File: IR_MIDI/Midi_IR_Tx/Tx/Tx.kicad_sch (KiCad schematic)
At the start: 16 parts, among them J1 MIDI in, J2 MIDI Thr, Q1 2N3904, Q2 2N3904, Q3 2N3904, Q4 2N3904, Y1 1MHz

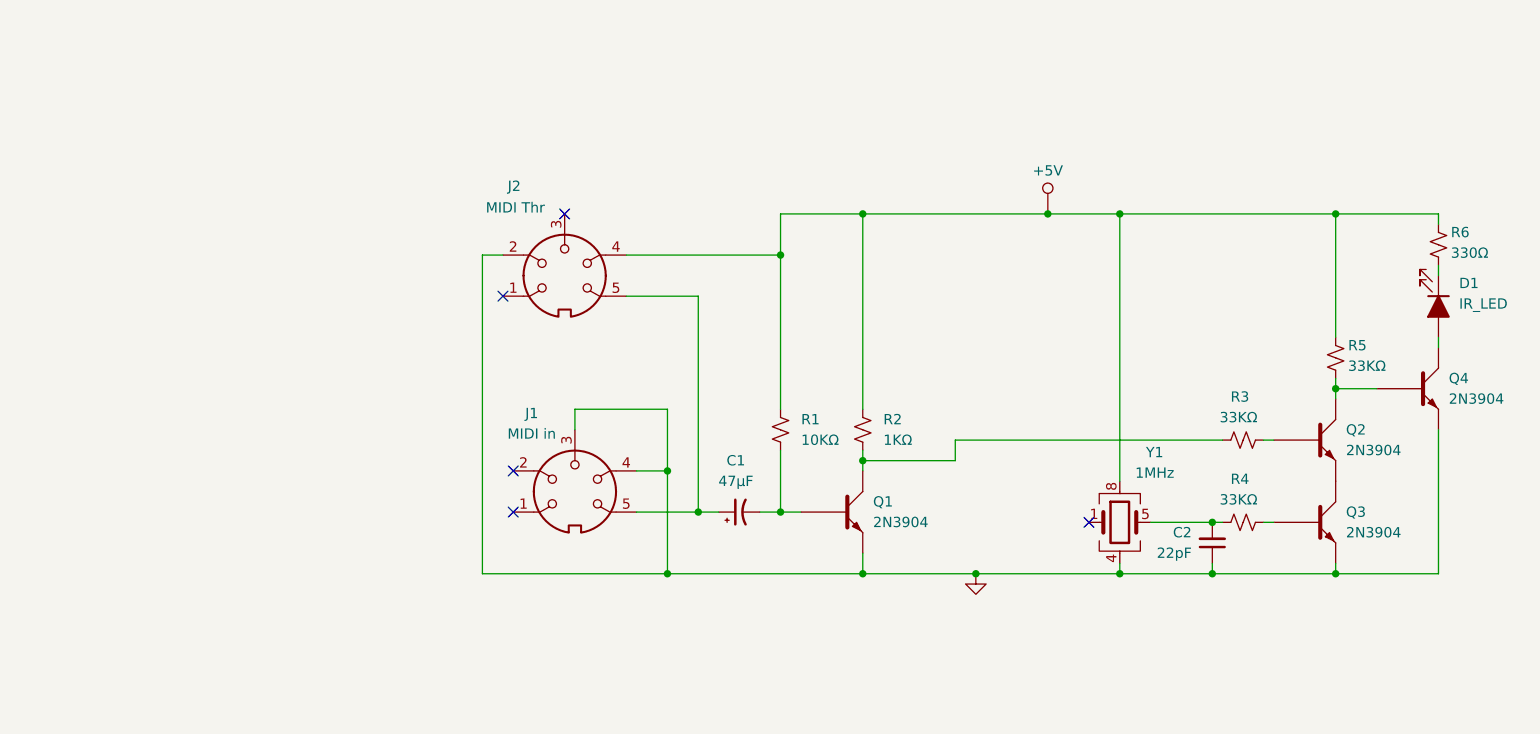
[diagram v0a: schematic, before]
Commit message: updated file structures and refreshed MIDI circuits
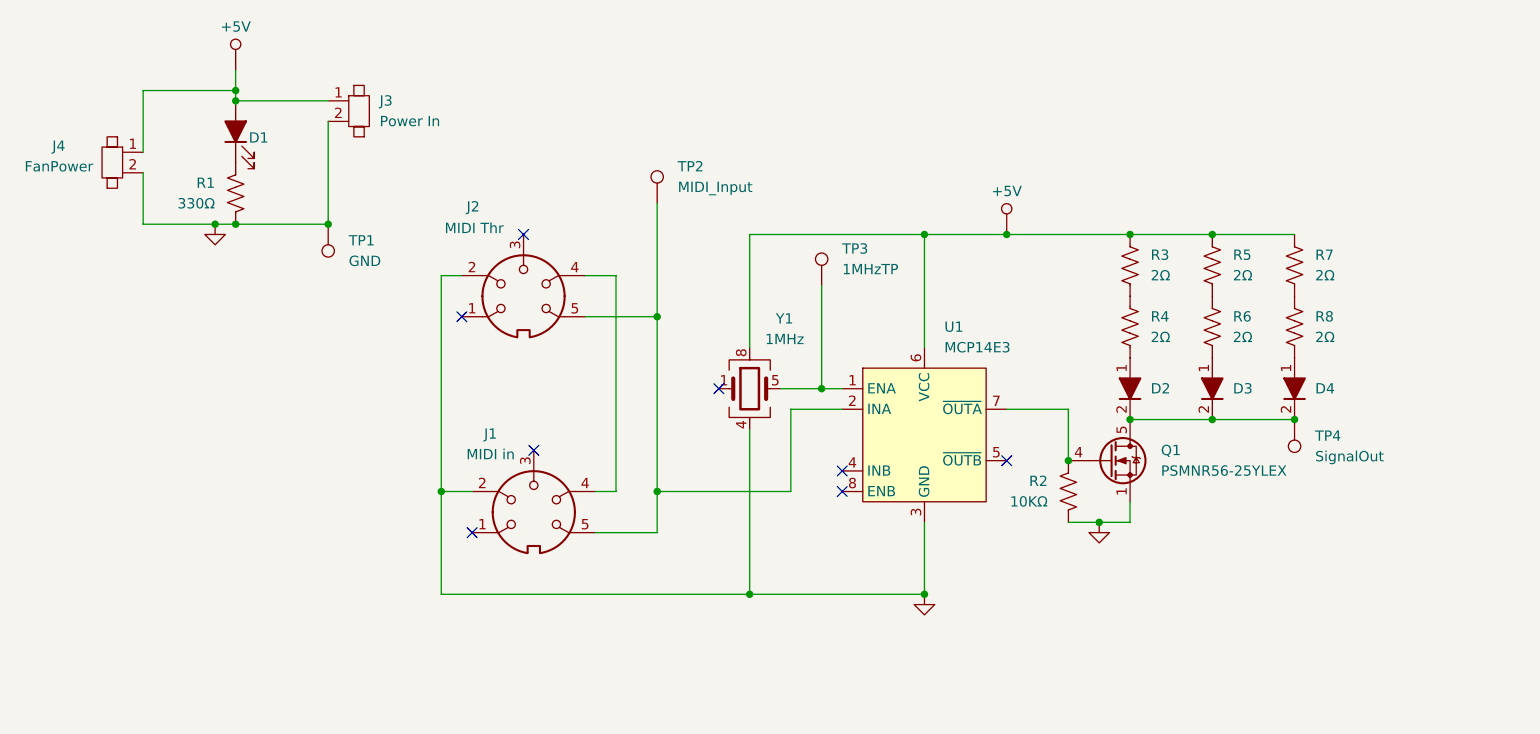
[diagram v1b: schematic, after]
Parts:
- removed C1: 47µF, symbol Device:C_Polarized_Small_US
- removed C2: 22pF, 2JB_Footprints:C_0805, symbol Device:C_Small
- removed Q1, Q2, Q3, Q4: 2N3904, Package_TO_SOT_THT:TO-92_Inline, symbol Transistor_BJT:2N3904
- removed R1: 10KΩ, 2JB_Footprints:C_0805, symbol Device:R_Small_US
- removed R2: 1KΩ, 2JB_Footprints:C_0805, symbol Device:R_Small_US
- removed R3, R4, R5: 33KΩ, 2JB_Footprints:C_0805, symbol Device:R_Small_US
- removed R6: 330Ω, 2JB_Footprints:C_0805, symbol Device:R_Small_US
- added D2, D3, D4: D_Filled, 2JB_Footprints:Fat_2Pin_D, symbol Device:D_Filled
- added J3: Power In, Connector_AMASS:AMASS_XT30U-F_1x02_P5.0mm_Vertical, symbol 2_JB_Custom_sym:Jumper_2_Pin
- added J4: FanPower, 2JB_Footprints:1X2_100mil_Header, symbol 2_JB_Custom_sym:Jumper_2_Pin
- added Q1: PSMNR56-25YLEX, Package_TO_SOT_SMD:LFPAK56, symbol Transistor_FET:PSMN5R2-60YL
- added R1: 330Ω, 2JB_Footprints:C_0805, symbol Device:R_US
- added R2: 10KΩ, 2JB_Footprints:C_0805, symbol Device:R_US
- added R3, R4, R5, R6, R7, R8: 2Ω, Package_TO_SOT_THT:TO-220-2_Vertical, symbol Device:R_US
- added TP1: GND, 2JB_Footprints:1X1_100mil_Header, symbol Connector:TestPoint
- added TP2: MIDI_Input, 2JB_Footprints:1X1_100mil_Header, symbol Connector:TestPoint
- added TP3: 1MHzTP, 2JB_Footprints:1X1_100mil_Header, symbol Connector:TestPoint
- added TP4: SignalOut, 2JB_Footprints:1X1_100mil_Header, symbol Connector:TestPoint
- added U1: MCP14E3, Package_SO:SOIC-8_3.9x4.9mm_P1.27mm, symbol 2_JB_Custom_sym:MCP14E3
- D1: value IR_LED -> LED_Filled
- J1, J2: footprint (none) -> 2JB_Footprints:DIN-5PIN_MIDI
- Y1: footprint (none) -> 2JB_Footprints:300x300Mil_4Pin_Y
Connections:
- net GND: now also J1.2, J3.2, J4.2, Q1.1 (S), Q1.2 (S), Q1.3 (S), R1.2, R2.2, TP1.1, U1.3 (GND); no longer J1.3, J1.4
- net at D1.1 (K): now also R1.1
- net at D1.2 (A): now also J3.1, J4.1
- net at Y1.8: now also R3.1, R5.1, R7.1, U1.6 (VCC); no longer J2.4
- net at J1.5, J2.5: now also TP2.1, U1.2 (INA)
- net at Y1.5: now also TP3.1, U1.1 (ENA)
- new net: R7.2, R8.1
- new net: D4.1 (A), R8.2
- new net: Q1.4 (G), R2.1, U1.7 (~{OUTA})
- new net: R5.2, R6.1
- new net: D2.2 (K), D3.2 (K), D4.2 (K), Q1.5 (D), TP4.1
- new net: R3.2, R4.1
- new net: D2.1 (A), R4.2
- new net: D3.1 (A), R6.2
- new net: J1.4, J2.4
- no-connect marks 5 -> 8
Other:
- moved on the sheet: J1, J2, Y1

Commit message: revised IR Tx board
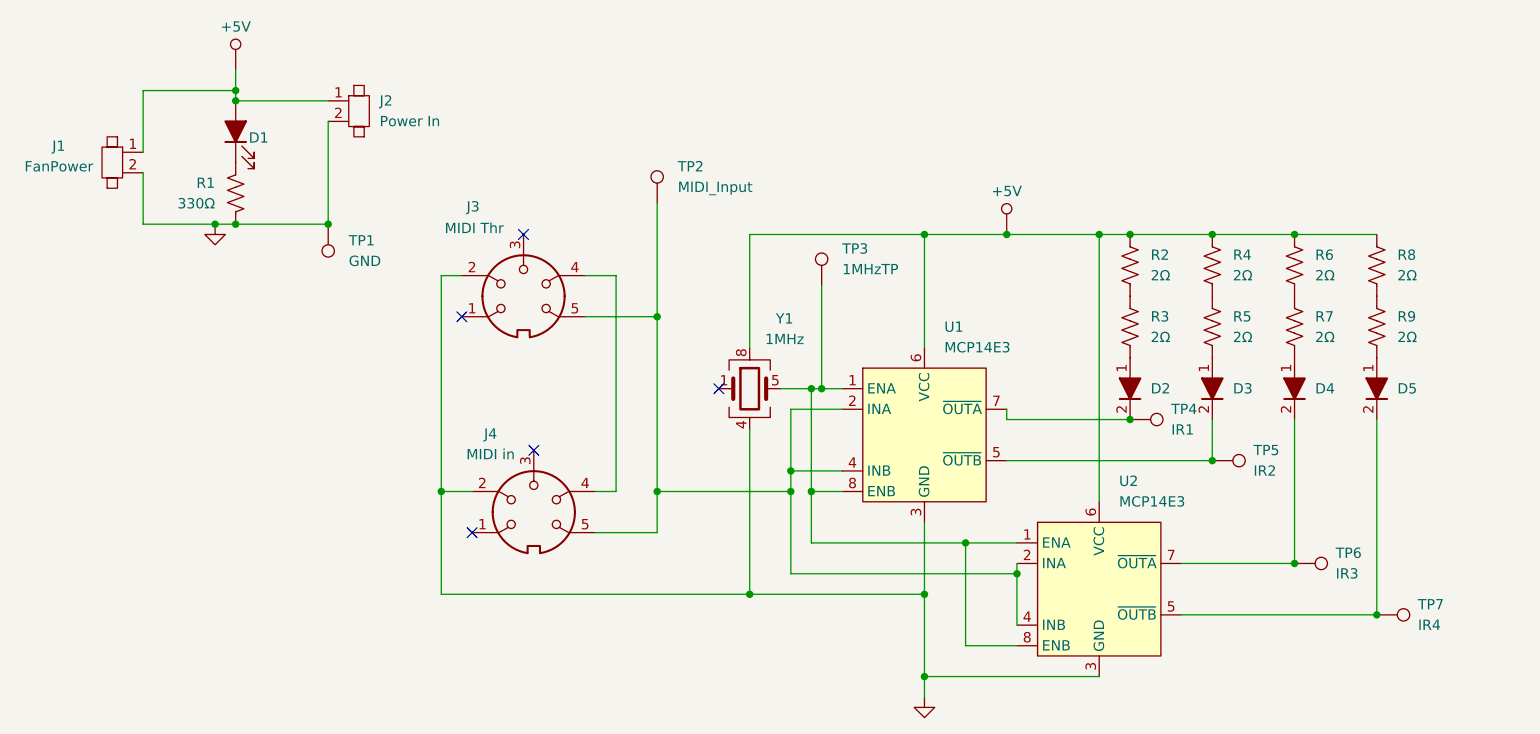
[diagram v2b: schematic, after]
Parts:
- removed Q1: PSMNR56-25YLEX, Package_TO_SOT_SMD:LFPAK56, symbol Transistor_FET:PSMN5R2-60YL
- removed R2: 10KΩ, 2JB_Footprints:C_0805, symbol Device:R_US
- added D5: D_Filled, 2JB_Footprints:Fat_2Pin_D, symbol Device:D_Filled
- added R8, R9: 2Ω, Package_TO_SOT_THT:TO-220-2_Vertical, symbol Device:R_US
- added TP5: IR2, 2JB_Footprints:1X1_100mil_Header, symbol Connector:TestPoint
- added TP6: IR3, 2JB_Footprints:1X1_100mil_Header, symbol Connector:TestPoint
- added TP7: IR4, 2JB_Footprints:1X1_100mil_Header, symbol Connector:TestPoint
- added U2: MCP14E3, Package_SO:SOIC-8_3.9x4.9mm_P1.27mm, symbol 2_JB_Custom_sym:MCP14E3
- TP4: value SignalOut -> IR1
- renumbered J4 to J1, J3 to J2, J2 to J3, J1 to J4, R3 to R2, R4 to R3, R5 to R4, R6 to R5, R7 to R6, R8 to R7
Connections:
- net GND: now also U2.3 (GND)
- net at U1.7 (~{OUTA}): now also D2.2 (K), TP4.1
- net at R2.1, R4.1, R6.1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: now also R8.1, U2.6 (VCC)
- net at TP3.1, U1.1 (ENA), Y1.5: now also U1.8 (ENB), U2.1 (ENA), U2.8 (ENB)
- net at J3.5, J4.5, TP2.1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: now also U1.4 (INB), U2.2 (INA), U2.4 (INB)
- net at U1.5 (~{OUTB}): now also D3.2 (K), TP5.1
- new net: D5.1 (A), R9.2
- new net: D5.2 (K), TP7.1, U2.5 (~{OUTB})
- new net: D4.2 (K), TP6.1, U2.7 (~{OUTA})
- new net: R8.2, R9.1
- no-connect marks 8 -> 5
